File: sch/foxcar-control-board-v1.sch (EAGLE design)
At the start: 84 parts, among them J1 MICROSD, J2 XBEE-PRO, J3 USB_MICROB_PLUG-PTH, U1 SPX29300, U2 VNH5019, U3 MPU6000, U4 HMC5883LSMD, U5 STM32F4V

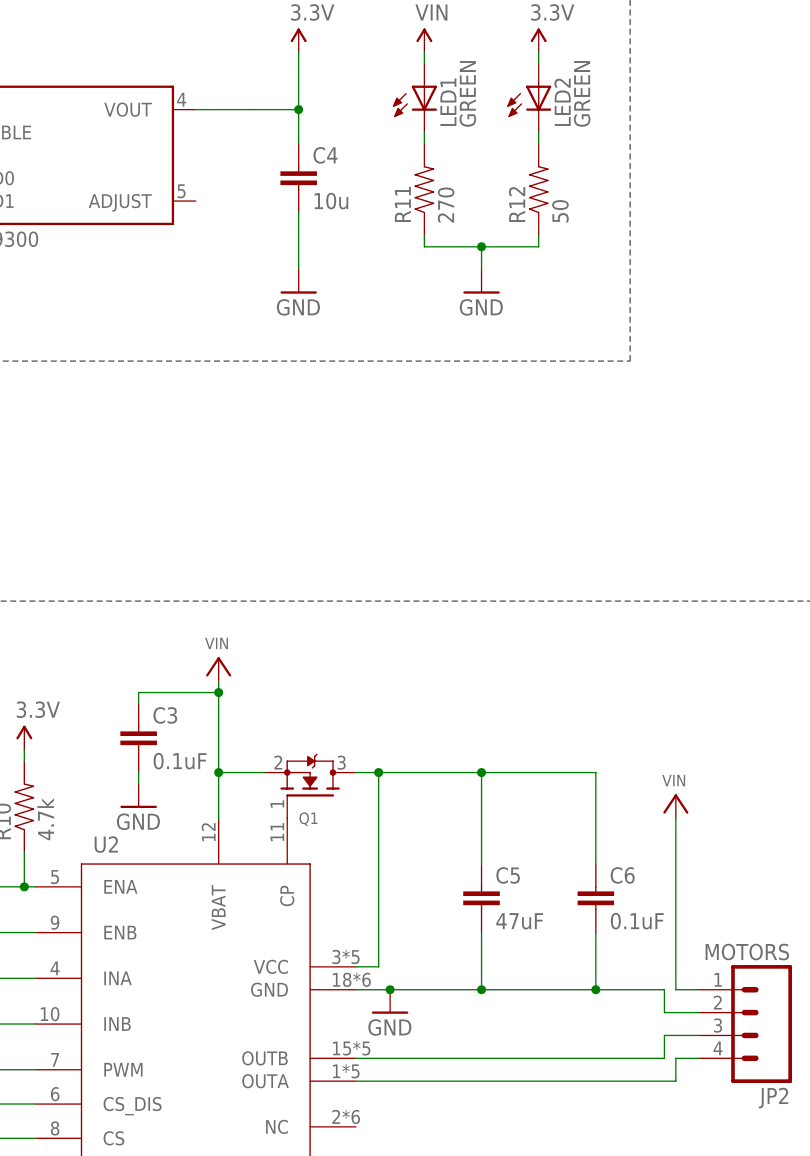
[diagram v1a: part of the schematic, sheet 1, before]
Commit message: Made BOM and had to make some changes. Final parts list included.
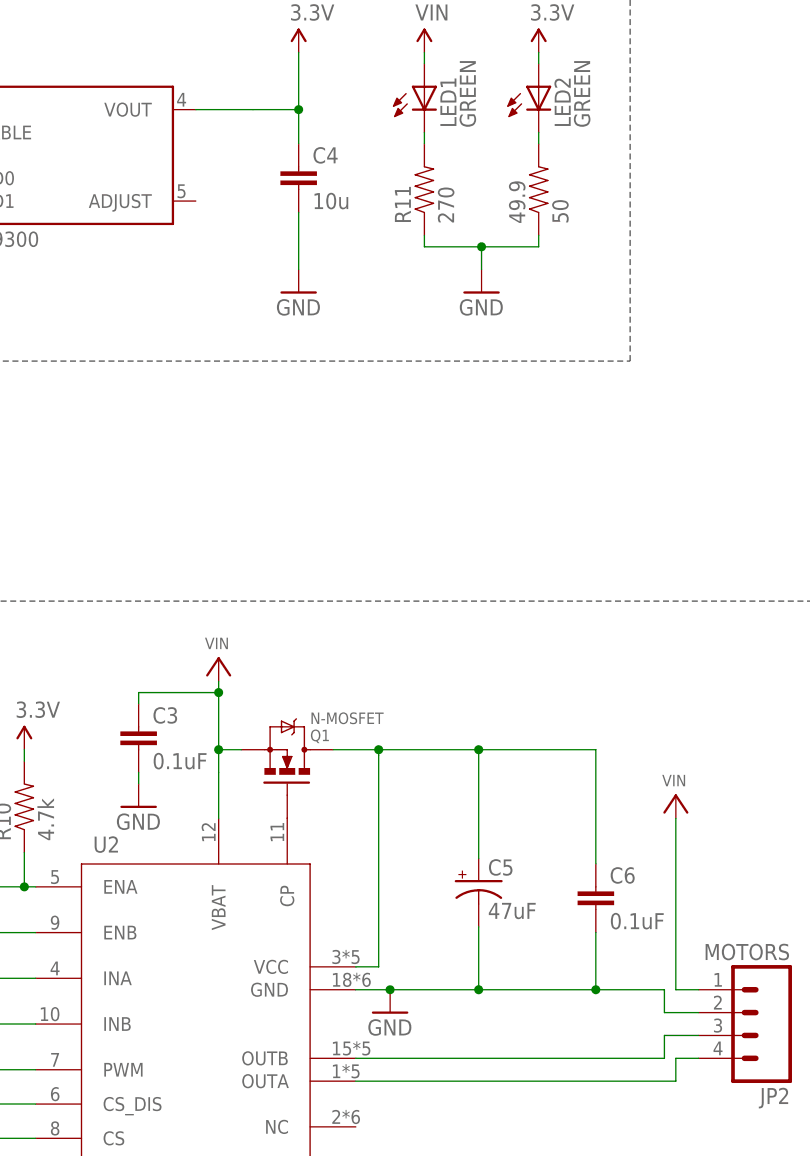
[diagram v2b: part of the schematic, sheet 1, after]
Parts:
- C1, C14, C15: device SparkFun-Passives:CAP0603-CAP -> SparkFun-Passives:CAP0402-CAP
- C11: device SparkFun-Passives:CAP0805 -> SparkFun-Passives:CAP0402-CAP
- C16, C19: value 16pF -> 15pF
- C5: device SparkFun-Passives:CAP0805 -> SparkFun-Passives:CAP_POLD
- J3: value USB_MICROB_PLUG-PTH -> CON-USB-F-MICRO-B; device SparkFun:USB_MICROB_PLUG-PTH -> dp_devices:CON-USB-F-MICRO-B
- Q1: value (none) -> N-MOSFET; device adafruit:MOSFET-NREFLOW -> SparkFun-DiscreteSemi:MOSFET-NCHANNELPTH2
- R1, R11: device SparkFun-Passives:RESISTOR0402-RES -> SparkFun-Passives:RESISTOR0603-RES
- R17, R18, R19: value 50 -> 49.9
- renumbered R12 to 49.9
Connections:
- net FS_DM: now also J3USB.D-; no longer J3.D-
- net FS_DP: now also J3USB.D+; no longer J3.D+
- net FS_ID: now also J3USB.USBID; no longer J3.ID
- net FS_VBUS: now also J3USB.VUSB; no longer J3.VCC
- net GND: now also C5.-, J3USB.GND; no longer C5.2, J3.GND
- net VCC: now also C5.+; no longer C5.1
